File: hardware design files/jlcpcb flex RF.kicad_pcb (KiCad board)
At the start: 2 copper layers, 100 x 100 mm, 24 parts, among them J1 SMA, J10 SMA, J11 SMA, J12 SMA, J13 SMA, J14 SMA, J15 SMA, J16 SMA, J2 SMA, J3 SMA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

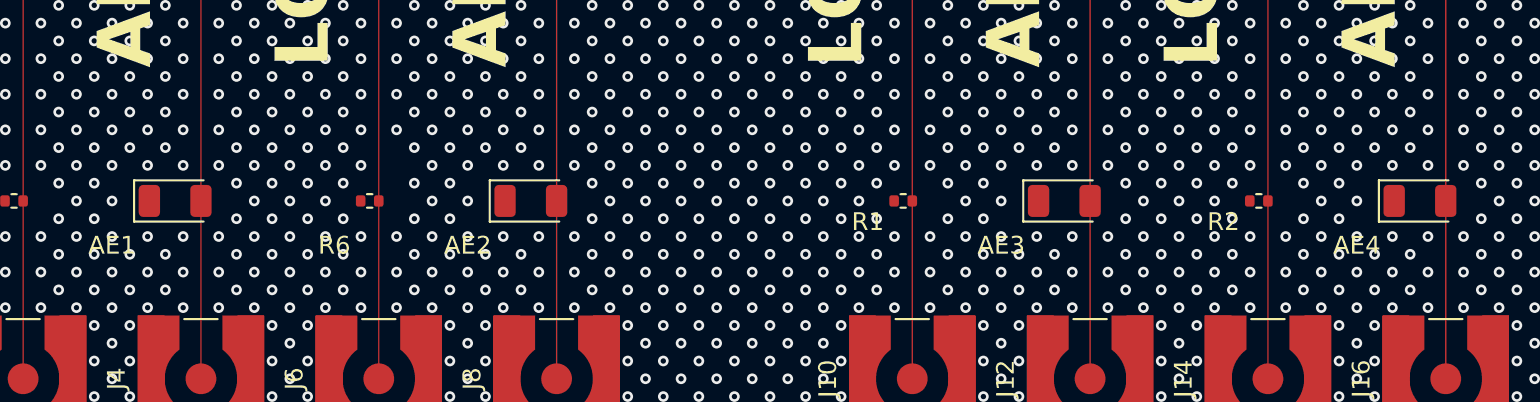
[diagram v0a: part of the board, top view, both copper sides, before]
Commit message: Antenna Ground Plane Openings
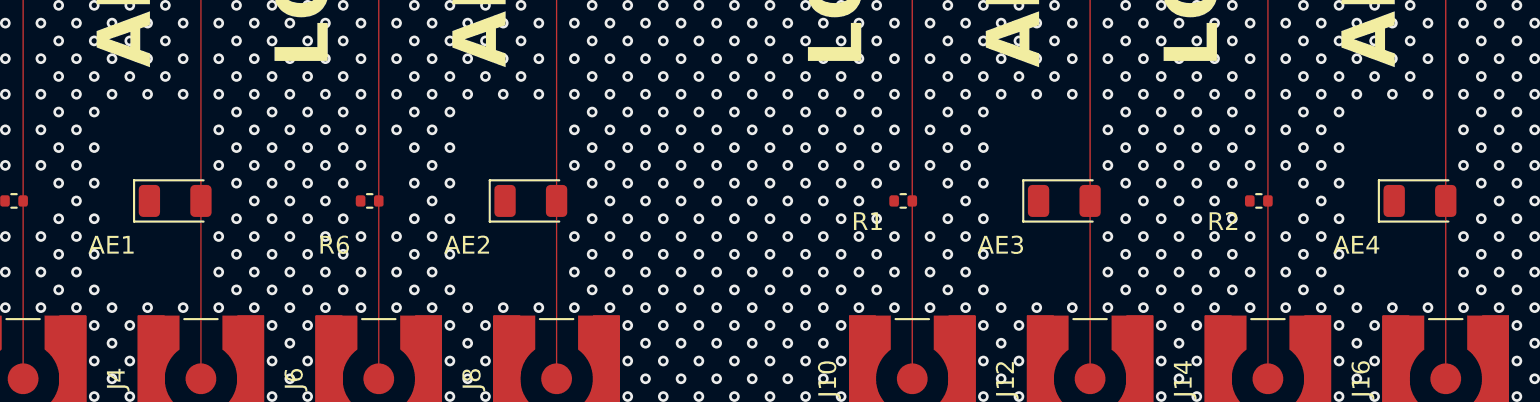
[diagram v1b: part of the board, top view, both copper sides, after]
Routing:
- net GND: vias 4152 -> 4068
